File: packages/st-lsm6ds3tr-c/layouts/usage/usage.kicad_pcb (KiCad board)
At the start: 2 copper layers, 6 parts

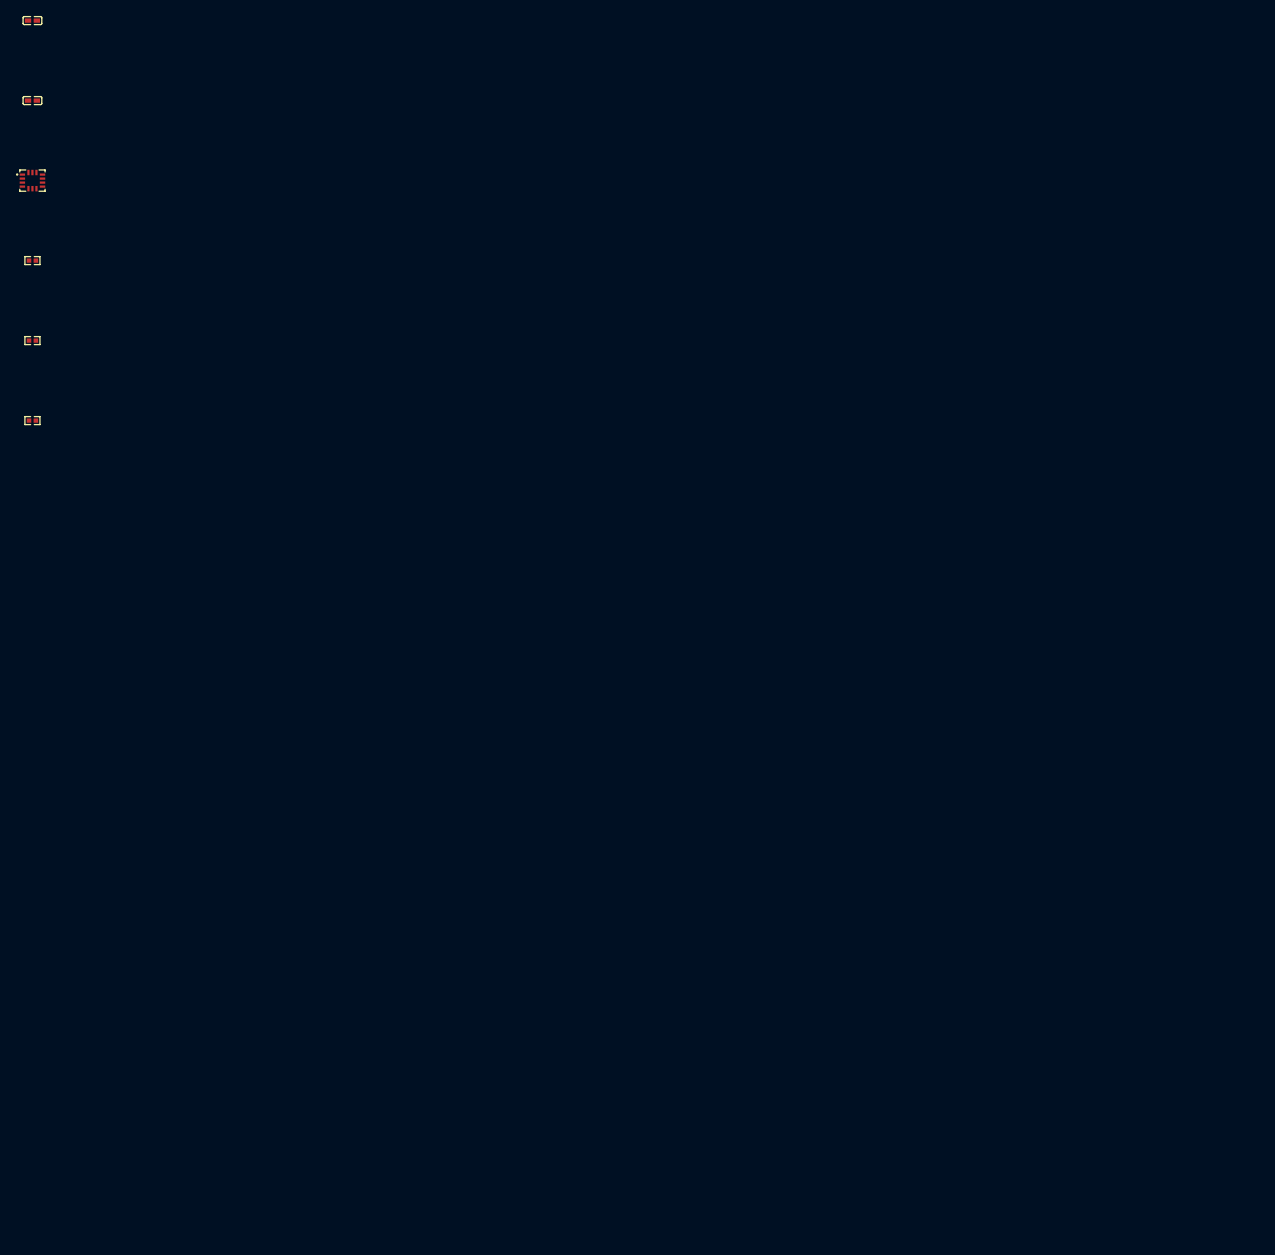
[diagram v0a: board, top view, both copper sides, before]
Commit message: deleting double package
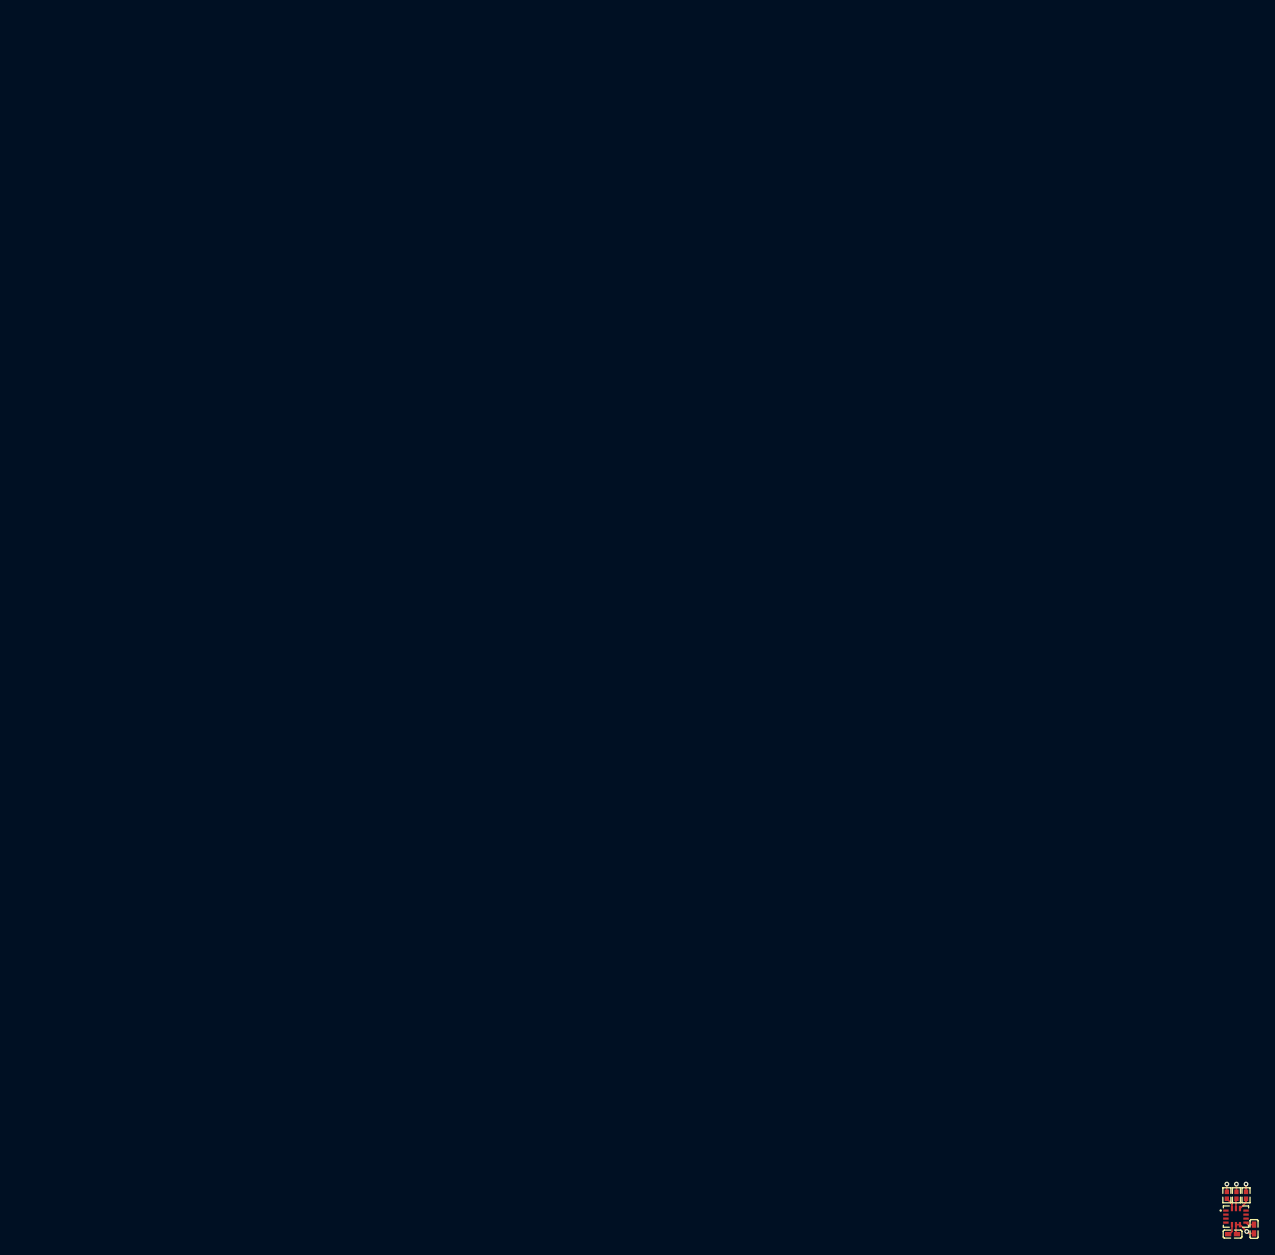
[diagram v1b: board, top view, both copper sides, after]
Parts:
- moved C2 214.8 mm to (152.7, 101.0), turned to -90 degrees
- moved C1 206.4 mm to (150.0, 101.7)
- moved U1 198.5 mm to (150.4, 99.5)
- moved R3 189.6 mm to (149.3, 96.8), turned to 90 degrees
- moved R2 184.6 mm to (150.5, 96.8), turned to 90 degrees
- moved R1 180.0 mm to (151.7, 96.8), turned to 90 degrees
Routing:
- net VCC: track 0.00 -> 5.34 mm, vias 0 -> 3
- net GND: track 0.00 -> 4.01 mm, vias 0 -> 1
- net CS: track 0.00 -> 1.99 mm
- net SDA: track 0.00 -> 1.49 mm
- net SCL: track 0.00 -> 1.25 mm

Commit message: st-lsm6ds3tr-c: package update to v0.2.0, ato:^0.14.0 (#288)
* st-lsm6ds3tr-c: package update to v0.2.0, ato:^0.14.0

Build targets:
  default = rc0
  usage = rc0
Package Verify: rc0
Version: 0.1.1 -> 0.2.0
Requires ato: ^0.14.0

* Update main.yml from main

Syncs GitHub Actions workflow configuration.

* ci: update workflow from main (fix package publish git issue)

---------

Co-authored-by: Nicholas Krstevski <nick@atopile.io>
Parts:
- C1, C2: value 100nF ±10% 16V X7R -> 1F
- R1, R2, R3: value 10kΩ ±1% 62.5mW -> 10000Ω
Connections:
- net INT1 renamed 4
- net INT2 renamed 9
- net VCC renamed hv
- C1 pad 2: GND -> lv
- C2 pad 2: GND -> lv
- U1 pad 1: address_bit_0 -> lv
- U1 pad 10: footprint-net-0 -> (no net)
- U1 pad 11: footprint-net-1 -> (no net)
- U1 pad 6: GND -> lv
- U1 pad 7: GND -> lv
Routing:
- net GND: track 4.01 -> 0.00 mm, vias 1 -> 0
- net 2: track 0.00 -> 4.01 mm, vias 0 -> 1
